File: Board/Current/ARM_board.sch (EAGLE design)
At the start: 175 parts, among them IC3 STM32F437VI, IC4 LM358DT, J1 USART/I2C, J10 ANALOG, J11 DGND, J12 DPWR, J13 DIGITAL, J14 SGND, J15 SPWR, J16 SERVO, J2 I2C2/USART3, J3 USART2, J5 SPI, J6 Bluesmirf, J7 SWD, J8 AGND, J9 APWR, Q1 STL4P2UH7, Q2 2STR1230, Q3 STL4P2UH7, SW1 SW, U1 LSM330, U10 BAV99, U11 BAV99, U12 USBLC6-2, U13 USBLC6-2, U14 STMPS2171MTR, U15 MC74HC164, U3 NC7SZU04, U4 L6206Q, U5 L6206Q, U6 SI7617, U7 SI7617, U8 SI7617, U9 SI7617, Y2 8MHz

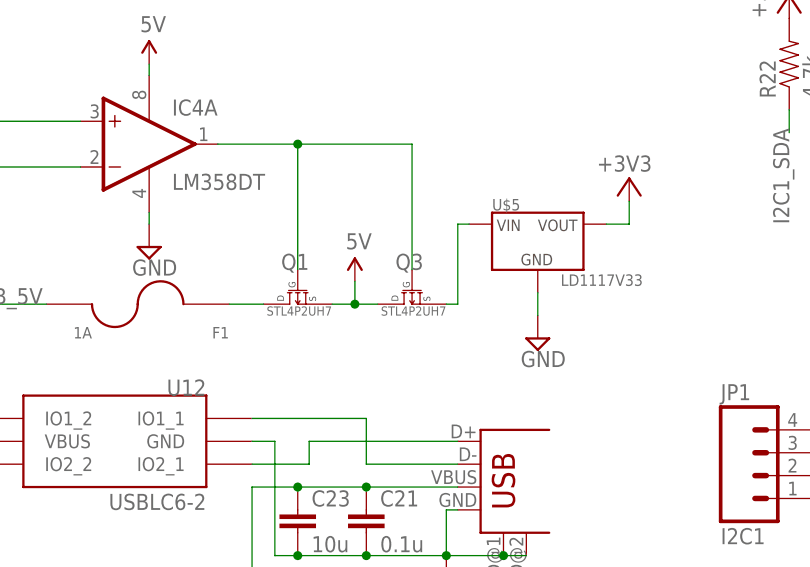
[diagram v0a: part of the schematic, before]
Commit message: Switched Q3 around. Minor layout tweaks.
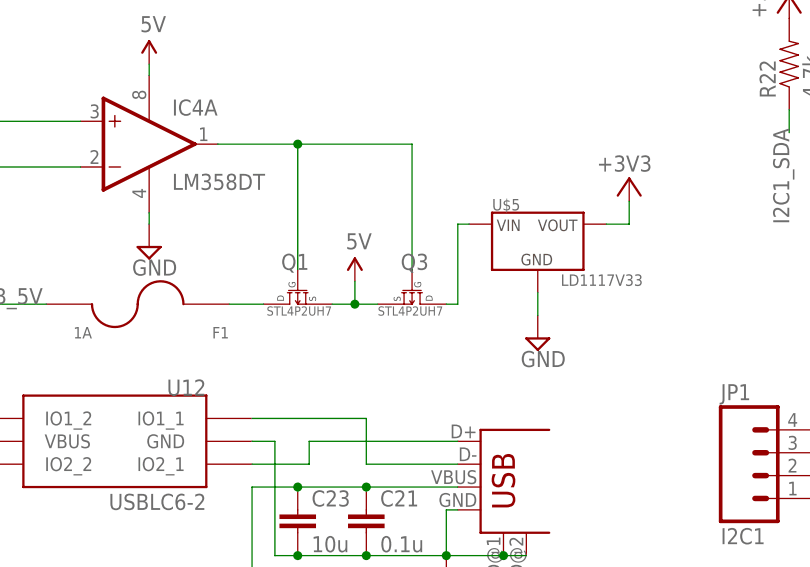
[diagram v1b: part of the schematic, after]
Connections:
- net 5V: now also Q3.S; no longer Q3.D
- net N$22: now also Q3.D; no longer Q3.S
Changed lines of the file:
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@@
 <setting verticaltext="up"/>
 </settings>
-<grid distance="0.1" unitdist="inch" unit="inch" style="lines" multiple="1" display="no" altdistance="0.01" altunitdist="inch" altunit="inch"/>
+<grid distance="0.05" unitdist="inch" unit="inch" style="lines" multiple="1" display="no" altdistance="0.01" altunitdist="inch" altunit="inch"/>
 <layers>
 <layer number="1" name="Top" color="4" fill="1" visible="no" active="no"/>
@@
 </instance>
 <instance part="U$5" gate="G$1" x="351.79" y="276.86"/>
-<instance part="Q3" gate="G$1" x="337.82" y="271.78" smashed="yes" rot="R270">
-<attribute name="NAME" x="339.09" y="274.32" size="1.778" layer="95" rot="MR0"/>
-<attribute name="VALUE" x="341.63" y="269.24" size="1.016" layer="96" rot="MR0"/>
+<instance part="Q3" gate="G$1" x="337.82" y="271.78" smashed="yes" rot="MR270">
+<attribute name="NAME" x="336.55" y="274.32" size="1.778" layer="95"/>
+<attribute name="VALUE" x="334.01" y="269.24" size="1.016" layer="96"/>
 </instance>
 <instance part="U$6" gate="G$1" x="331.47" y="273.05"/>
@@
 <wire x1="328.93" y1="270.51" x2="331.47" y2="270.51" width="0.1524" layer="91"/>
 <wire x1="331.47" y1="270.51" x2="331.47" y2="273.05" width="0.1524" layer="91"/>
-<pinref part="Q3" gate="G$1" pin="D"/>
-<wire x1="331.47" y1="270.51" x2="334.01" y2="270.51" width="0.1524" layer="91"/>
+<pinref part="Q3" gate="G$1" pin="S"/>
+<wire x1="334.01" y1="270.51" x2="331.47" y2="270.51" width="0.1524" layer="91"/>
 <junction x="331.47" y="270.51"/>
 </segment>
@@
 <net name="N$22" class="0">
 <segment>
-<pinref part="Q3" gate="G$1" pin="S"/>
 <pinref part="U$5" gate="G$1" pin="VIN"/>
-<wire x1="341.63" y1="270.51" x2="342.9" y2="270.51" width="0.1524" layer="91"/>
 <wire x1="342.9" y1="270.51" x2="342.9" y2="279.4" width="0.1524" layer="91"/>
 <wire x1="342.9" y1="279.4" x2="344.17" y2="279.4" width="0.1524" layer="91"/>
+<pinref part="Q3" gate="G$1" pin="D"/>
+<wire x1="341.63" y1="270.51" x2="342.9" y2="270.51" width="0.1524" layer="91"/>
 </segment>
 </net>

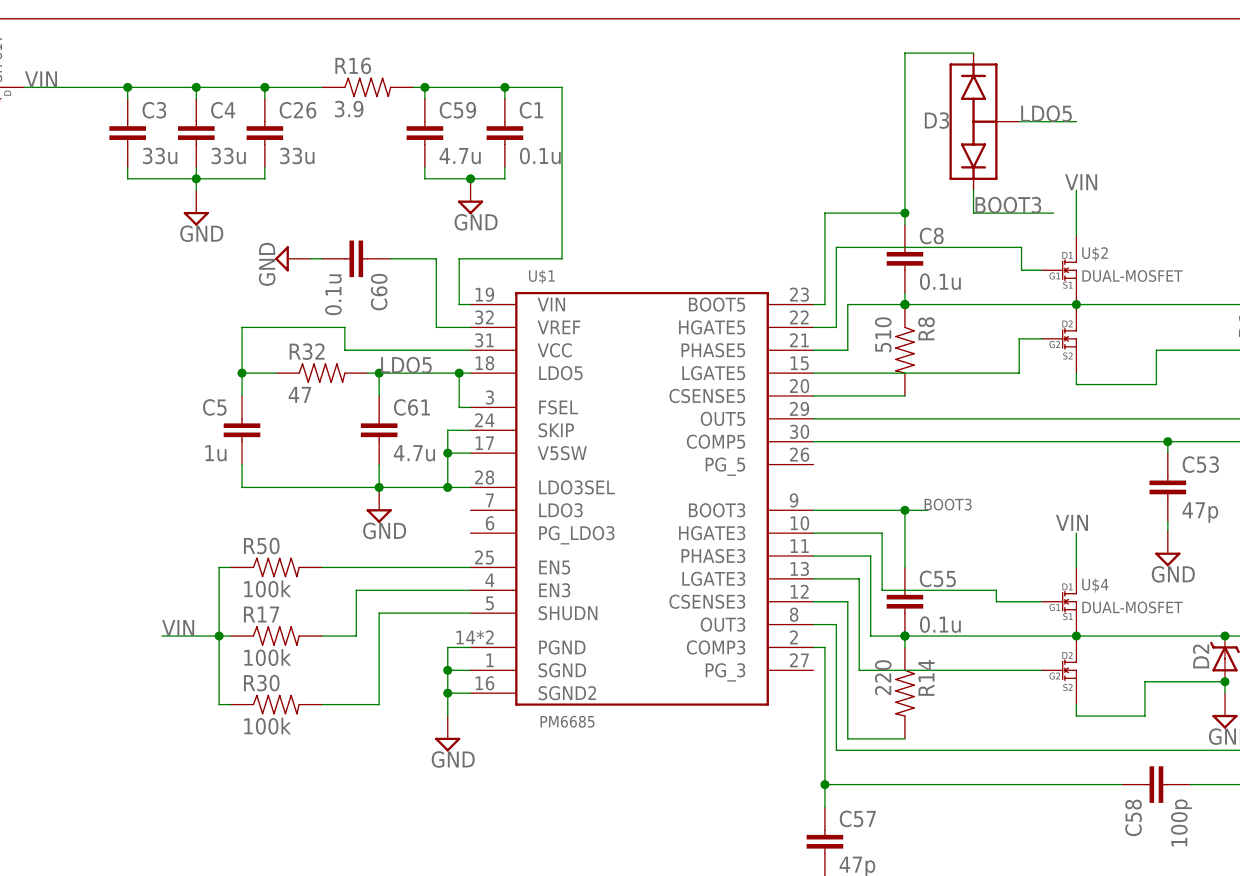
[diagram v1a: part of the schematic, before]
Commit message: Addressed switching regulator comments.
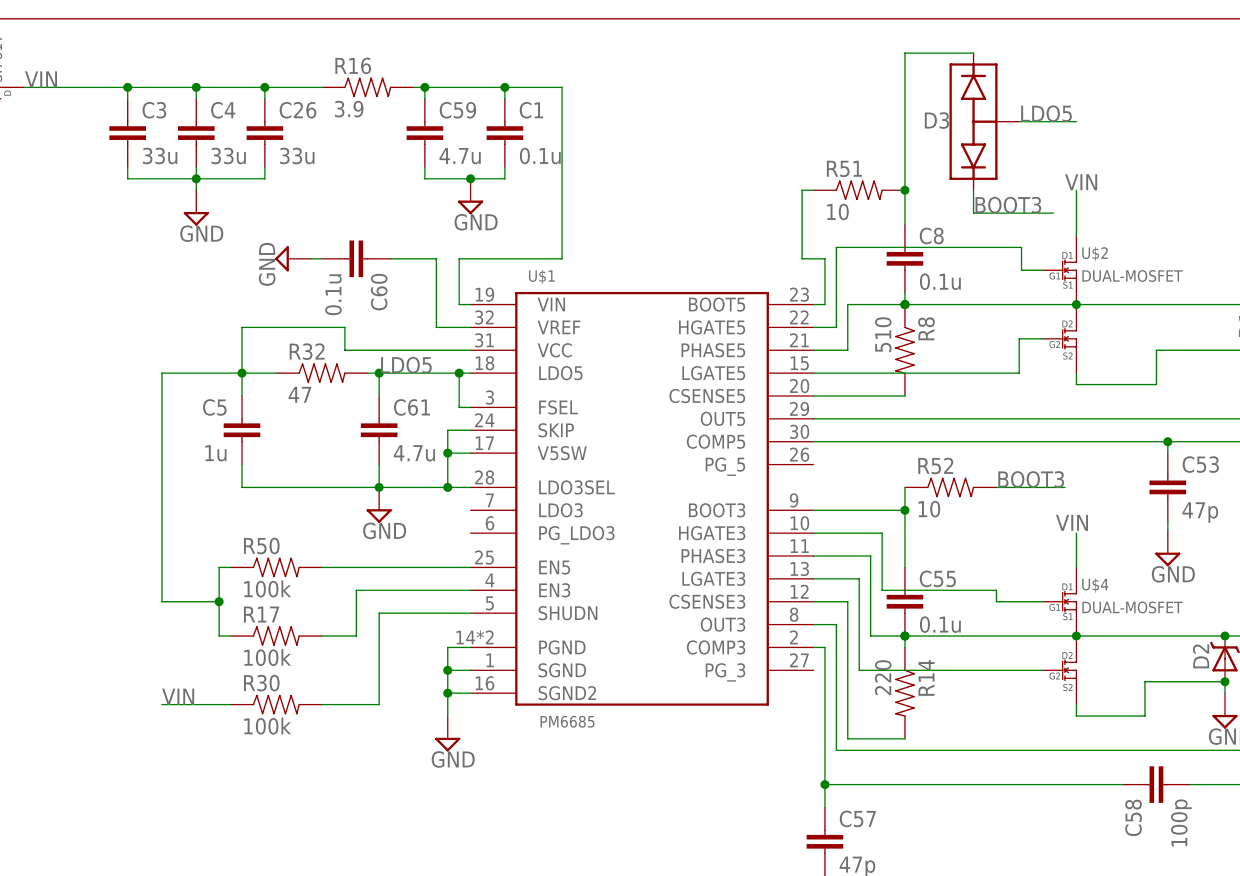
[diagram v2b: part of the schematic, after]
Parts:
- added R51, R52: 10, SparkFun:RESISTOR0402-RES
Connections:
- new net N$15: C5.1, R17.1, R32.1, R50.1, U$1.VCC
- new net N$59: C55.1, R52.1, U$1.BOOT3
- net BOOT3: now also R52.2; no longer C55.1, U$1.BOOT3
- net N$20: now also R51.1, U$1.BOOT5; no longer C5.1, R32.1, U$1.VCC
- net N$25: now also R51.2; no longer U$1.BOOT5
- net VIN: no longer R17.1, R50.1
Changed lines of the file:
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@@
 <part name="SUPPLY74" library="supply2" deviceset="GND" device=""/>
 <part name="U$7" library="SparkFun" deviceset="5V" device=""/>
+<part name="R51" library="SparkFun" deviceset="RESISTOR" device="0402-RES" value="10"/>
+<part name="R52" library="SparkFun" deviceset="RESISTOR" device="0402-RES" value="10"/>
 </parts>
 <sheets>
@@
 <instance part="SUPPLY74" gate="GND" x="284.48" y="270.51"/>
 <instance part="U$7" gate="G$1" x="284.48" y="298.45"/>
+<instance part="R51" gate="G$1" x="144.78" y="290.83"/>
+<instance part="R52" gate="G$1" x="154.94" y="257.81"/>
 </instances>
 <busses>
@@
 <segment>
 <pinref part="R30" gate="G$1" pin="1"/>
-<wire x1="74.93" y1="233.68" x2="73.66" y2="233.68" width="0.1524" layer="91"/>
-<wire x1="73.66" y1="233.68" x2="73.66" y2="241.3" width="0.1524" layer="91"/>
-<wire x1="73.66" y1="241.3" x2="73.66" y2="248.92" width="0.1524" layer="91"/>
-<pinref part="R17" gate="G$1" pin="1"/>
-<wire x1="74.93" y1="241.3" x2="73.66" y2="241.3" width="0.1524" layer="91"/>
-<junction x="73.66" y="241.3"/>
-<pinref part="R50" gate="G$1" pin="1"/>
-<wire x1="74.93" y1="248.92" x2="73.66" y2="248.92" width="0.1524" layer="91"/>
-<label x="67.31" y="241.3" size="1.778" layer="95"/>
-<wire x1="73.66" y1="241.3" x2="67.31" y2="241.3" width="0.1524" layer="91"/>
+<label x="67.31" y="233.68" size="1.778" layer="95"/>
+<wire x1="74.93" y1="233.68" x2="67.31" y2="233.68" width="0.1524" layer="91"/>
 </segment>
 <segment>
@@
 </segment>
 </net>
-<net name="N$20" class="0">
-<segment>
-<pinref part="U$1" gate="G$1" pin="VCC"/>
-<wire x1="76.2" y1="275.59" x2="87.63" y2="275.59" width="0.1524" layer="91"/>
-<wire x1="87.63" y1="275.59" x2="87.63" y2="273.05" width="0.1524" layer="91"/>
-<wire x1="87.63" y1="273.05" x2="101.6" y2="273.05" width="0.1524" layer="91"/>
-<pinref part="R32" gate="G$1" pin="1"/>
-<wire x1="80.01" y1="270.51" x2="76.2" y2="270.51" width="0.1524" layer="91"/>
-<wire x1="76.2" y1="270.51" x2="76.2" y2="275.59" width="0.1524" layer="91"/>
-<pinref part="C5" gate="G$1" pin="1"/>
-<wire x1="76.2" y1="270.51" x2="76.2" y2="267.97" width="0.1524" layer="91"/>
-<junction x="76.2" y="270.51"/>
-</segment>
-</net>
 <net name="N$25" class="0">
 <segment>
-<wire x1="149.86" y1="287.02" x2="149.86" y2="288.29" width="0.1524" layer="91"/>
 <pinref part="C8" gate="G$1" pin="1"/>
-<junction x="149.86" y="288.29"/>
-<pinref part="U$1" gate="G$1" pin="BOOT5"/>
-<wire x1="140.97" y1="278.13" x2="139.7" y2="278.13" width="0.1524" layer="91"/>
-<wire x1="149.86" y1="288.29" x2="140.97" y2="288.29" width="0.1524" layer="91"/>
-<wire x1="140.97" y1="288.29" x2="140.97" y2="278.13" width="0.1524" layer="91"/>
 <pinref part="D3" gate="G$1" pin="P$1"/>
 <wire x1="157.48" y1="306.07" x2="149.86" y2="306.07" width="0.1524" layer="91"/>
-<wire x1="149.86" y1="306.07" x2="149.86" y2="288.29" width="0.1524" layer="91"/>
+<wire x1="149.86" y1="306.07" x2="149.86" y2="290.83" width="0.1524" layer="91"/>
+<pinref part="R51" gate="G$1" pin="2"/>
+<wire x1="149.86" y1="290.83" x2="149.86" y2="287.02" width="0.1524" layer="91"/>
+<junction x="149.86" y="290.83"/>
 </segment>
 </net>
@@
 <net name="BOOT3" class="0">
 <segment>
-<wire x1="152.4" y1="255.27" x2="149.86" y2="255.27" width="0.1524" layer="91"/>
-<pinref part="U$1" gate="G$1" pin="BOOT3"/>
-<pinref part="C55" gate="G$1" pin="1"/>
-<wire x1="149.86" y1="255.27" x2="139.7" y2="255.27" width="0.1524" layer="91"/>
-<wire x1="149.86" y1="255.27" x2="149.86" y2="248.92" width="0.1524" layer="91"/>
-<junction x="149.86" y="255.27"/>
-<label x="151.892" y="255.27" size="1.27" layer="95"/>
-</segment>
-<segment>
 <pinref part="D3" gate="G$1" pin="P$2"/>
 <wire x1="157.48" y1="290.83" x2="157.48" y2="288.29" width="0.1524" layer="91"/>
@@
 <label x="157.48" y="288.29" size="1.778" layer="95"/>
 </segment>
+<segment>
+<pinref part="R52" gate="G$1" pin="2"/>
+<wire x1="160.02" y1="257.81" x2="167.64" y2="257.81" width="0.1524" layer="91"/>
+<label x="160.02" y="257.81" size="1.778" layer="95"/>
+</segment>
 </net>
 <net name="N$10" class="0">
@@
 </segment>
 </net>
+<net name="N$15" class="0">
+<segment>
+<pinref part="R50" gate="G$1" pin="1"/>
+<wire x1="74.93" y1="248.92" x2="73.66" y2="248.92" width="0.1524" layer="91"/>
+<pinref part="R17" gate="G$1" pin="1"/>
+<wire x1="74.93" y1="241.3" x2="73.66" y2="241.3" width="0.1524" layer="91"/>
+<wire x1="73.66" y1="241.3" x2="73.66" y2="245.11" width="0.1524" layer="91"/>
+<wire x1="73.66" y1="245.11" x2="67.31" y2="245.11" width="0.1524" layer="91"/>
+<wire x1="73.66" y1="248.92" x2="73.66" y2="245.11" width="0.1524" layer="91"/>
+<wire x1="67.31" y1="245.11" x2="67.31" y2="270.51" width="0.1524" layer="91"/>
+<pinref part="U$1" gate="G$1" pin="VCC"/>
+<wire x1="76.2" y1="275.59" x2="87.63" y2="275.59" width="0.1524" layer="91"/>
+<wire x1="87.63" y1="275.59" x2="87.63" y2="273.05" width="0.1524" layer="91"/>
+<wire x1="87.63" y1="273.05" x2="101.6" y2="273.05" width="0.1524" layer="91"/>
+<pinref part="R32" gate="G$1" pin="1"/>
+<wire x1="80.01" y1="270.51" x2="76.2" y2="270.51" width="0.1524" layer="91"/>
+<wire x1="76.2" y1="270.51" x2="76.2" y2="275.59" width="0.1524" layer="91"/>
+<pinref part="C5" gate="G$1" pin="1"/>
+<wire x1="76.2" y1="270.51" x2="76.2" y2="267.97" width="0.1524" layer="91"/>
+<junction x="76.2" y="270.51"/>
+<wire x1="67.31" y1="270.51" x2="76.2" y2="270.51" width="0.1524" layer="91"/>
+<junction x="73.66" y="245.11"/>
+</segment>
+</net>
+<net name="N$20" class="0">
+<segment>
+<pinref part="U$1" gate="G$1" pin="BOOT5"/>
+<wire x1="140.97" y1="278.13" x2="139.7" y2="278.13" width="0.1524" layer="91"/>
+<pinref part="R51" gate="G$1" pin="1"/>
+<wire x1="139.7" y1="290.83" x2="138.43" y2="290.83" width="0.1524" layer="91"/>
+<wire x1="138.43" y1="290.83" x2="138.43" y2="283.21" width="0.1524" layer="91"/>
+<wire x1="138.43" y1="283.21" x2="140.97" y2="283.21" width="0.1524" layer="91"/>
+<wire x1="140.97" y1="283.21" x2="140.97" y2="278.13" width="0.1524" layer="91"/>
+</segment>
+</net>
+<net name="N$59" class="0">
+<segment>
+<pinref part="U$1" gate="G$1" pin="BOOT3"/>
+<wire x1="139.7" y1="255.27" x2="149.86" y2="255.27" width="0.1524" layer="91"/>
+<pinref part="R52" gate="G$1" pin="1"/>
+<wire x1="149.86" y1="257.81" x2="149.86" y2="255.27" width="0.1524" layer="91"/>
+<pinref part="C55" gate="G$1" pin="1"/>
+<wire x1="149.86" y1="255.27" x2="149.86" y2="248.92" width="0.1524" layer="91"/>
+<junction x="149.86" y="255.27"/>
+</segment>
+</net>
